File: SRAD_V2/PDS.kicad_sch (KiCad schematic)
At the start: 12 parts, among them J2 Conn_01x02_Pin, U2 TPS563200

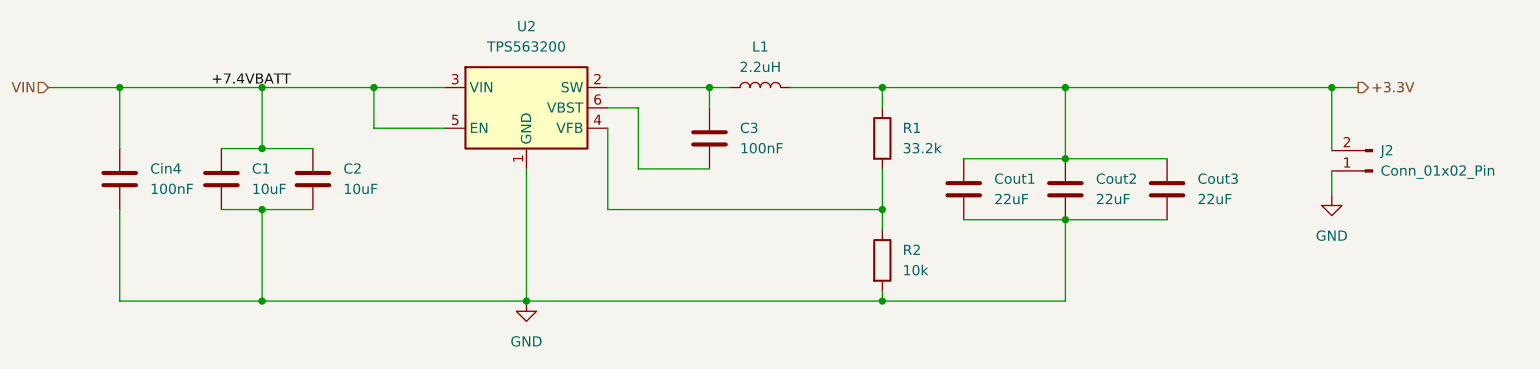
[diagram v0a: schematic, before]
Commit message: Merged the new schematic with the main project successfully!
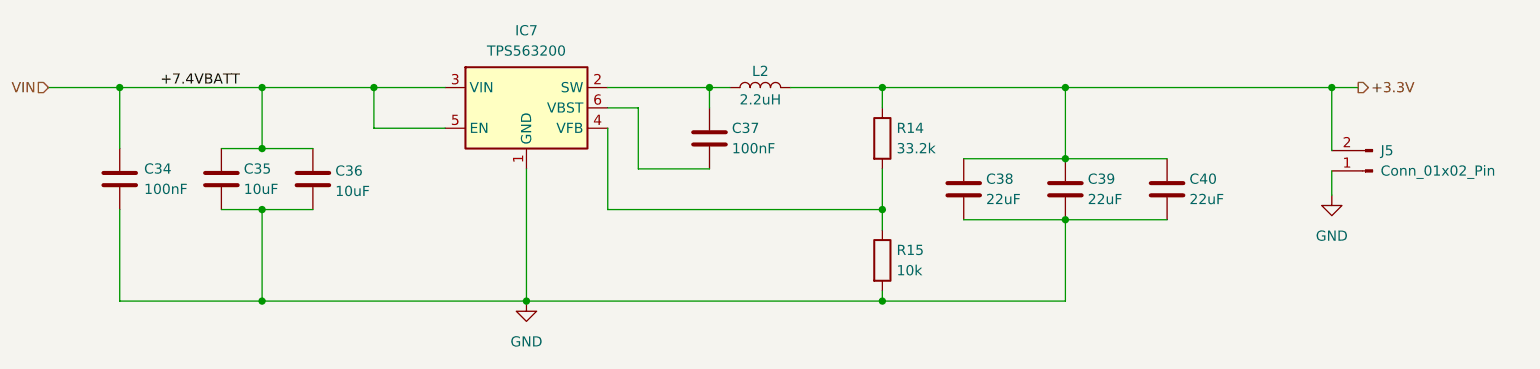
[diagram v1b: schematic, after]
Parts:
- renumbered Cin4 to C34, C1 to C35, C2 to C36, C3 to C37, Cout1 to C38, Cout2 to C39, Cout3 to C40, U2 to IC7, J2 to J5, L1 to L2, R1 to R14, R2 to R15
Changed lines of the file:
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@@
 	)
 	(label "+7.4VBATT"
-		(at 97.79 81.28 0)
+		(at 91.44 81.28 0)
 		(effects
 			(font
@@
 		(dnp no)
 		(fields_autoplaced yes)
-		(property "Reference" "#PWR037"
+		(property "Reference" "#PWR047"
 			(at 237.744 101.092 0)
 			(hide yes)
@@
 			(project "SRAD_V2"
 				(path "/016ea6e5-09c6-43d4-b6cc-3404e2d65458/9c8bbba4-8714-49e8-941c-914b77648ac5"
-					(reference "#PWR037")
+					(reference "#PWR047")
 					(unit 1)
 				)
@@
 		(in_pos_files yes)
 		(dnp no)
-		(fields_autoplaced yes)
-		(property "Reference" "Cout3"
-			(at 220.98 92.7099 0)
+		(property "Reference" "C40"
+			(at 219.964 92.71 0)
 			(show_name no)
 			(do_not_autoplace no)
@@
 		)
 		(property "Value" "22uF"
-			(at 220.98 95.2499 0)
+			(at 219.964 95.25 0)
 			(show_name no)
 			(do_not_autoplace no)
@@
 			(project "SRAD_V2"
 				(path "/016ea6e5-09c6-43d4-b6cc-3404e2d65458/9c8bbba4-8714-49e8-941c-914b77648ac5"
-					(reference "Cout3")
+					(reference "C40")
 					(unit 1)
 				)
@@
 		(in_pos_files yes)
 		(dnp no)
-		(fields_autoplaced yes)
-		(property "Reference" "L1"
-			(at 166.37 76.2 90)
+		(property "Reference" "L2"
+			(at 166.37 79.248 90)
 			(show_name no)
 			(do_not_autoplace no)
@@
 		)
 		(property "Value" "2.2uH"
-			(at 166.37 78.74 90)
+			(at 166.37 82.804 90)
 			(show_name no)
 			(do_not_autoplace no)
@@
 			(project "SRAD_V2"
 				(path "/016ea6e5-09c6-43d4-b6cc-3404e2d65458/9c8bbba4-8714-49e8-941c-914b77648ac5"
-					(reference "L1")
+					(reference "L2")
 					(unit 1)
 				)
@@
 		(dnp no)
 		(fields_autoplaced yes)
-		(property "Reference" "#PWR01"
+		(property "Reference" "#PWR046"
 			(at 137.16 114.3 0)
 			(hide yes)
@@
 			(project "SRAD_V2"
 				(path "/016ea6e5-09c6-43d4-b6cc-3404e2d65458/9c8bbba4-8714-49e8-941c-914b77648ac5"
-					(reference "#PWR01")
+					(reference "#PWR046")
 					(unit 1)
 				)
@@
 		(in_pos_files yes)
 		(dnp no)
-		(fields_autoplaced yes)
-		(property "Reference" "U2"
-			(at 137.16 73.66 0)
+		(property "Reference" "IC7"
+			(at 137.16 74.168 0)
 			(show_name no)
 			(do_not_autoplace no)
@@
 		)
 		(property "Value" "TPS563200"
-			(at 137.16 76.2 0)
+			(at 137.16 76.708 0)
 			(show_name no)
 			(do_not_autoplace no)
@@
 			(project "SRAD_V2"
 				(path "/016ea6e5-09c6-43d4-b6cc-3404e2d65458/9c8bbba4-8714-49e8-941c-914b77648ac5"
-					(reference "U2")
+					(reference "IC7")
 					(unit 1)
 				)
@@
 		(in_pos_files yes)
 		(dnp no)
-		(property "Reference" "Cout1"
-			(at 195.58 92.7099 0)
+		(property "Reference" "C38"
+			(at 194.564 92.71 0)
 			(show_name no)
 			(do_not_autoplace no)
@@
 		)
 		(property "Value" "22uF"
-			(at 195.58 95.2499 0)
+			(at 194.564 95.25 0)
 			(show_name no)
 			(do_not_autoplace no)
@@
 			(project "SRAD_V2"
 				(path "/016ea6e5-09c6-43d4-b6cc-3404e2d65458/9c8bbba4-8714-49e8-941c-914b77648ac5"
-					(reference "Cout1")
+					(reference "C38")
 					(unit 1)
 				)
@@
 		(in_pos_files yes)
 		(dnp no)
-		(fields_autoplaced yes)
-		(property "Reference" "C3"
-			(at 163.83 86.3599 0)
+		(property "Reference" "C37"
+			(at 162.814 86.36 0)
 			(show_name no)
 			(do_not_autoplace no)
@@
 		)
 		(property "Value" "100nF"
-			(at 163.83 88.8999 0)
+			(at 162.814 88.9 0)
 			(show_name no)
 			(do_not_autoplace no)
@@
 			(project "SRAD_V2"
 				(path "/016ea6e5-09c6-43d4-b6cc-3404e2d65458/9c8bbba4-8714-49e8-941c-914b77648ac5"
-					(reference "C3")
+					(reference "C37")
 					(unit 1)
 				)
@@
 		(in_pos_files yes)
 		(dnp no)
-		(fields_autoplaced yes)
-		(property "Reference" "R2"
-			(at 184.15 101.5999 0)
+		(property "Reference" "R15"
+			(at 183.388 101.6 0)
 			(show_name no)
 			(do_not_autoplace no)
@@
 		)
 		(property "Value" "10k"
-			(at 184.15 104.1399 0)
+			(at 183.388 104.14 0)
 			(show_name no)
 			(do_not_autoplace no)
@@
 			(project "SRAD_V2"
 				(path "/016ea6e5-09c6-43d4-b6cc-3404e2d65458/9c8bbba4-8714-49e8-941c-914b77648ac5"
-					(reference "R2")
+					(reference "R15")
 					(unit 1)
 				)
@@
 		(in_pos_files yes)
 		(dnp no)
-		(fields_autoplaced yes)
-		(property "Reference" "R1"
-			(at 184.15 86.3599 0)
+		(property "Reference" "R14"
+			(at 183.388 86.36 0)
 			(show_name no)
 			(do_not_autoplace no)
@@
 		)
 		(property "Value" "33.2k"
-			(at 184.15 88.8999 0)
+			(at 183.388 88.9 0)
 			(show_name no)
 			(do_not_autoplace no)
@@
 			(project "SRAD_V2"
 				(path "/016ea6e5-09c6-43d4-b6cc-3404e2d65458/9c8bbba4-8714-49e8-941c-914b77648ac5"
-					(reference "R1")
+					(reference "R14")
 					(unit 1)
 				)
@@
 		(dnp no)
 		(fields_autoplaced yes)
-		(property "Reference" "J2"
+		(property "Reference" "J5"
 			(at 243.84 89.1539 0)
 			(show_name no)
@@
 			(project "SRAD_V2"
 				(path "/016ea6e5-09c6-43d4-b6cc-3404e2d65458/9c8bbba4-8714-49e8-941c-914b77648ac5"
-					(reference "J2")
+					(reference "J5")
 					(unit 1)
 				)
@@
 		(in_pos_files yes)
 		(dnp no)
-		(fields_autoplaced yes)
-		(property "Reference" "C1"
-			(at 102.87 91.4399 0)
+		(property "Reference" "C35"
+			(at 101.854 91.44 0)
 			(show_name no)
 			(do_not_autoplace no)
@@
 		)
 		(property "Value" "10uF"
-			(at 102.87 93.9799 0)
+			(at 101.854 93.98 0)
 			(show_name no)
 			(do_not_autoplace no)
@@
 			(project "SRAD_V2"
 				(path "/016ea6e5-09c6-43d4-b6cc-3404e2d65458/9c8bbba4-8714-49e8-941c-914b77648ac5"
-					(reference "C1")
+					(reference "C35")
 					(unit 1)
 				)
@@
 		(in_pos_files yes)
 		(dnp no)
-		(fields_autoplaced yes)
-		(property "Reference" "Cout2"
-			(at 208.28 92.7099 0)
+		(property "Reference" "C39"
+			(at 207.264 92.71 0)
 			(show_name no)
 			(do_not_autoplace no)
@@
 		)
 		(property "Value" "22uF"
-			(at 208.28 95.2499 0)
+			(at 207.264 95.25 0)
 			(show_name no)
 			(do_not_autoplace no)
@@
 			(project "SRAD_V2"
 				(path "/016ea6e5-09c6-43d4-b6cc-3404e2d65458/9c8bbba4-8714-49e8-941c-914b77648ac5"
-					(reference "Cout2")
+					(reference "C39")
 					(unit 1)
 				)
@@
 		(in_pos_files yes)
 		(dnp no)
-		(fields_autoplaced yes)
-		(property "Reference" "Cin4"
-			(at 90.17 91.4399 0)
+		(property "Reference" "C34"
+			(at 89.408 91.44 0)
 			(show_name no)
 			(do_not_autoplace no)
@@
 		)
 		(property "Value" "100nF"
-			(at 90.17 93.9799 0)
+			(at 89.408 93.98 0)
 			(show_name no)
 			(do_not_autoplace no)
@@
 			(project "SRAD_V2"
 				(path "/016ea6e5-09c6-43d4-b6cc-3404e2d65458/9c8bbba4-8714-49e8-941c-914b77648ac5"
-					(reference "Cin4")
+					(reference "C34")
 					(unit 1)
 				)
@@
 		(in_pos_files yes)
 		(dnp no)
-		(fields_autoplaced yes)
-		(property "Reference" "C2"
-			(at 114.3 91.4399 0)
+		(property "Reference" "C36"
+			(at 113.284 91.694 0)
 			(show_name no)
 			(do_not_autoplace no)
@@
 		)
 		(property "Value" "10uF"
-			(at 114.3 93.9799 0)
+			(at 113.284 94.234 0)
 			(show_name no)
 			(do_not_autoplace no)
@@
 			(project "SRAD_V2"
 				(path "/016ea6e5-09c6-43d4-b6cc-3404e2d65458/9c8bbba4-8714-49e8-941c-914b77648ac5"
-					(reference "C2")
-					(unit 1)
-				)
+					(reference "C36")
+					(unit 1)
+				)

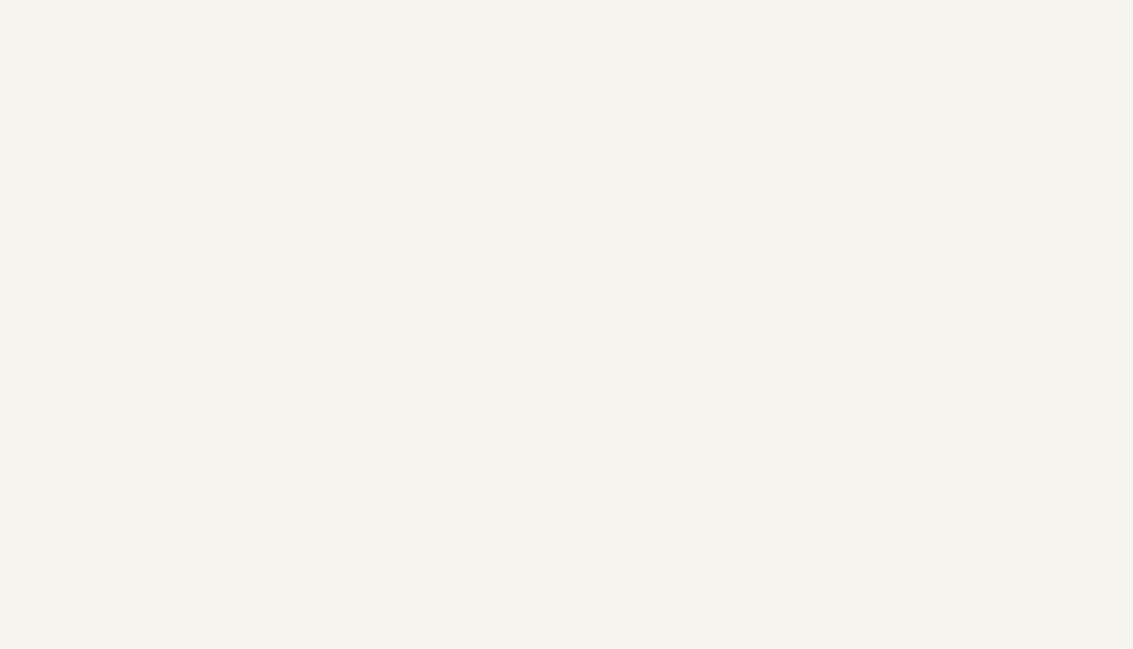
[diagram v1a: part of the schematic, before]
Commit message: In the process of adding an over discharge protection for PDS battery
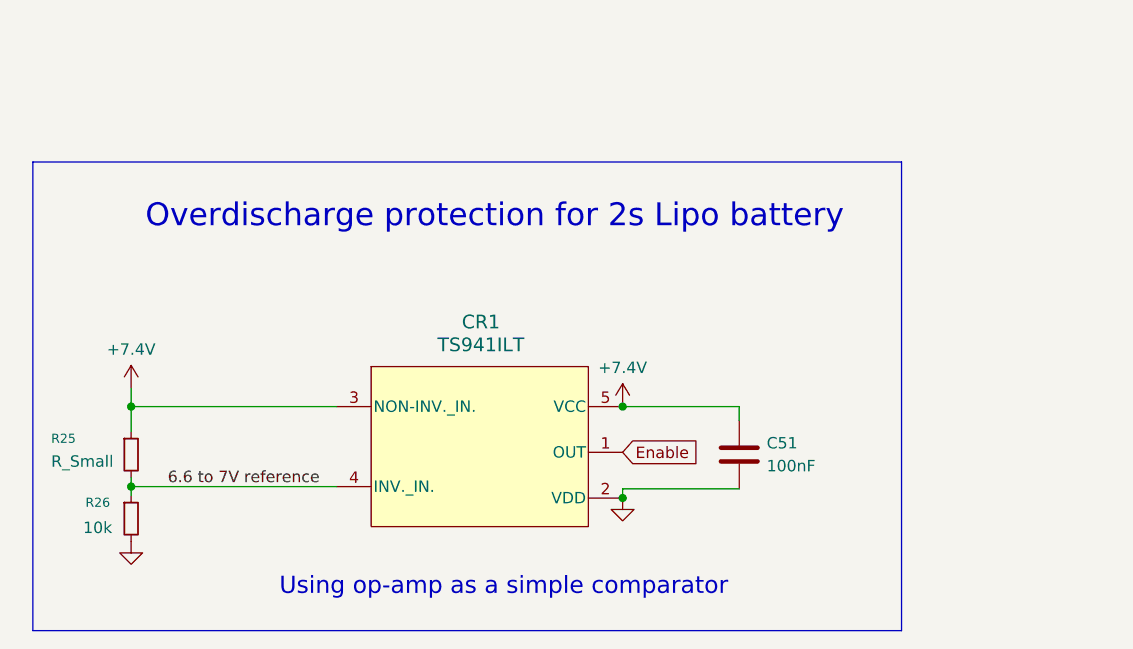
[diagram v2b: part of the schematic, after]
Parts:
- added C51: 100nF, Capacitor_SMD:C_0603_1608Metric, symbol Device:C
- added CR1: TS941ILT, TS941ILT:SOT23-5L_STM, symbol TS941ILT:TS941ILT
- added R25: R_Small, Resistor_SMD:R_0603_1608Metric, symbol Device:R_Small
- added R26: 10k, Resistor_SMD:R_0603_1608Metric, symbol Device:R_Small
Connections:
- net GND: now also C51.2, CR1.2 (VDD), R26.2
- new net +7.4V: C51.1, CR1.3 (NON-INV._IN.), CR1.5 (VCC), R25.1
- new net 6.6 to 7V reference: CR1.4 (INV._IN.), R25.2, R26.1
- new net Enable: CR1.1 (OUT)
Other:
- note added: "Overdischarge protection for 2s Lipo battery"
- note added: "Using op-amp as a simple comparator"
